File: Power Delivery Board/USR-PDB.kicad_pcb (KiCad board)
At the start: 2 copper layers, 100 x 150 mm, 19 parts, among them U10 Anderson PP45 Vert. 2x1, U11 Anderson PP45 Vert. 2x1, U12 TL2575HV-05IKV, U13 MCP3002-I/P, U2 LM2676T-12_NOPB, U5 Anderson PP45 Vert. 2x1, U6 Anderson PP45 Vert. 2x1, U7 Anderson PP45 Vert. 2x1, U8 Anderson PP45 Vert. 2x1, U9 Anderson PP45 Vert. 2x1

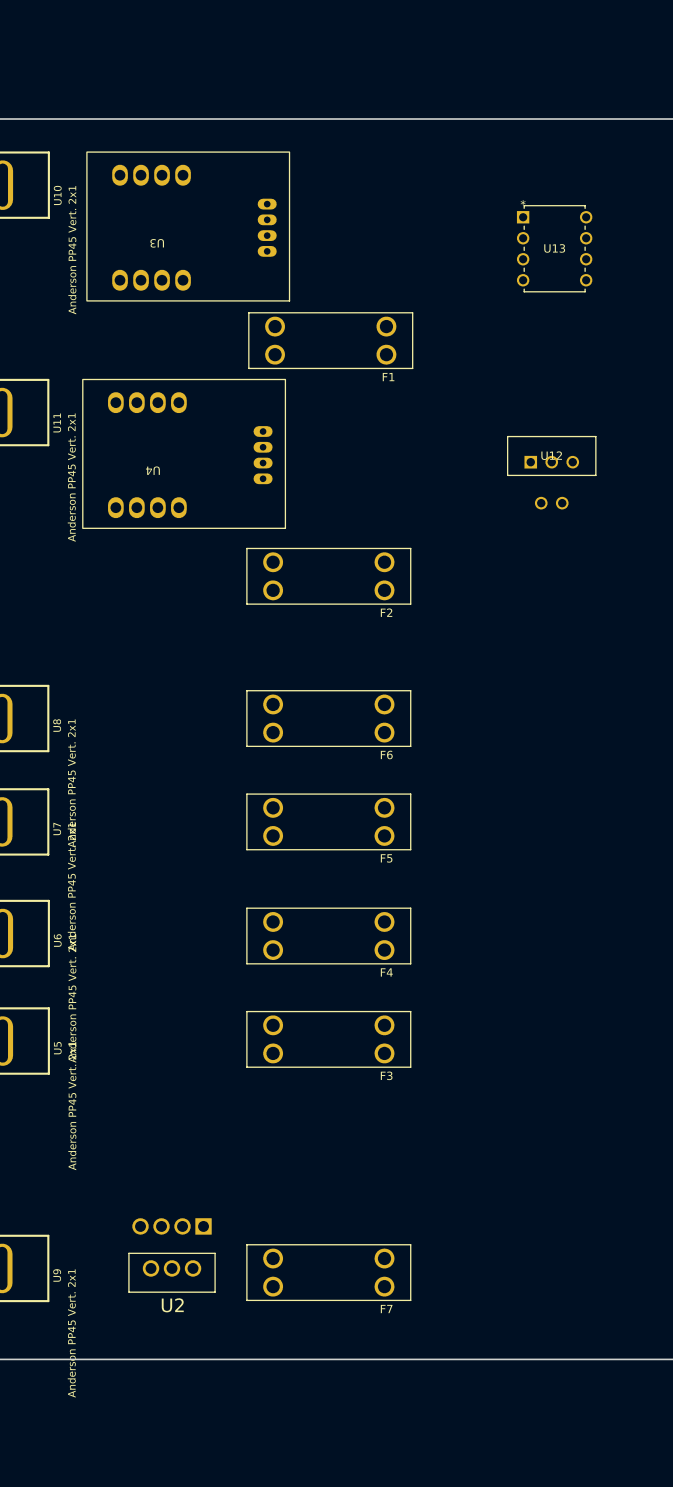
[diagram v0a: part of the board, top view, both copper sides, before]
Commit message: PDB: added footprint for D2
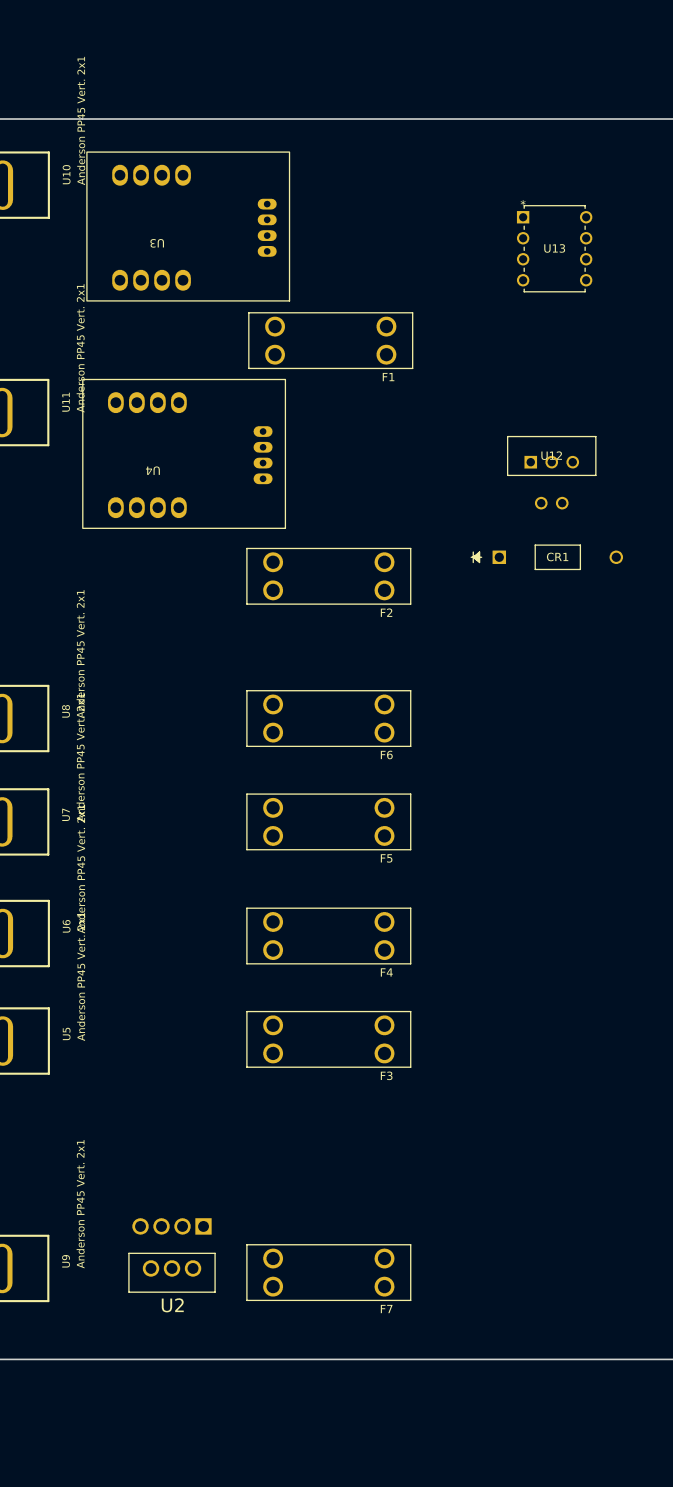
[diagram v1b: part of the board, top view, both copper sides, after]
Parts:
- added CR1: 1N5819, USR:DO-41_STM, F.Cu at (133.9, 75.5)
- F1, F2, F3, F4, F5, F6, F7: footprint USR-Footprint-Library:FUSE_3557-15 -> USR:FUSE_3557-15
- U10, U11, U5, U6, U7, U8, U9: footprint USR-Footprint-Library:ANDERSON PP45 VERT. 2X1 -> USR:ANDERSON PP45 VERT. 2X1
- U12: footprint USR-Footprint-Library:TL2575HV-05IKV -> USR:TL2575HV-05IKV
- U13: footprint USR-Footprint-Library:PDIP8_300MC_MCH -> USR:PDIP8_300MC_MCH
- U2: footprint USR-Footprint-Library:LM2676-TO127P457X1016X2052-7P -> USR:LM2676-TO127P457X1016X2052-7P
- U3, U4: footprint USR-Footprint-Library:LKSR 50-NP -> USR:LKSR 50-NP
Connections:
- net 5Vout renamed 5V

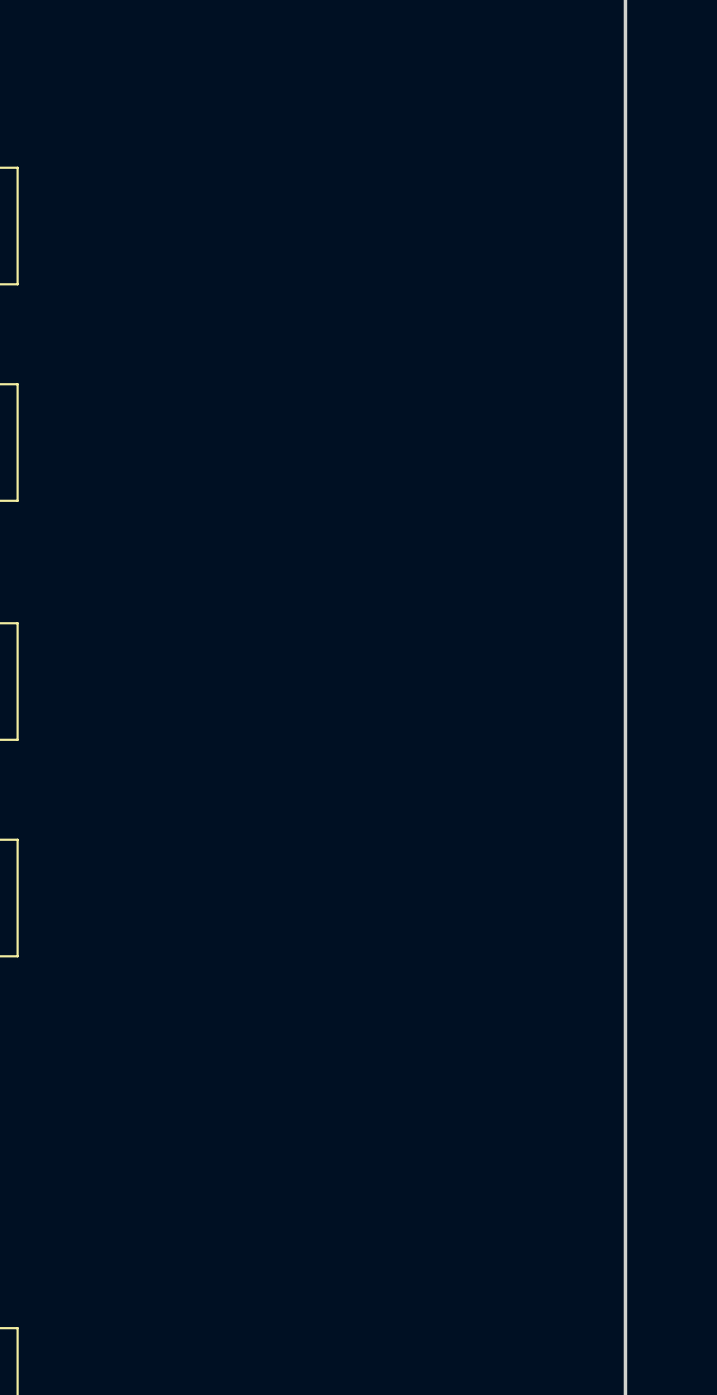
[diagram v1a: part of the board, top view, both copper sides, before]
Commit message: Added footprints and datasheets for capacitors, inductors, and diodes
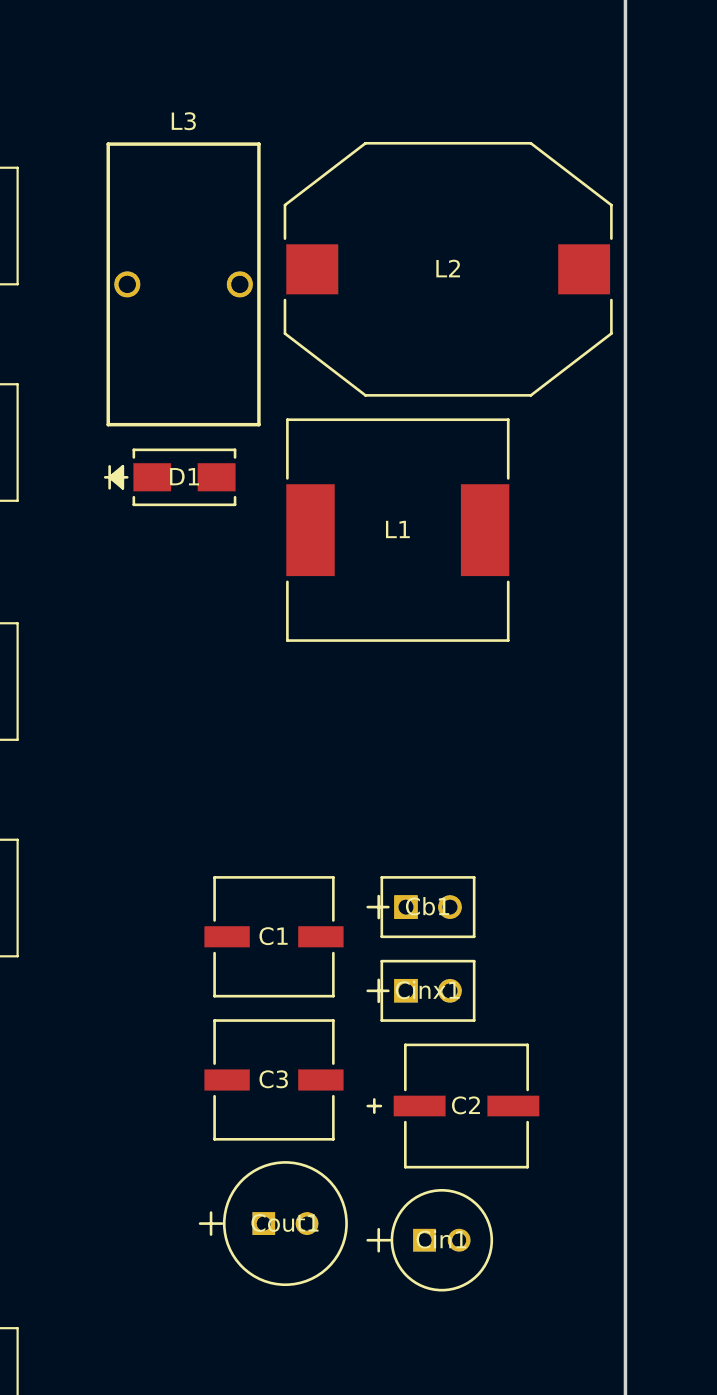
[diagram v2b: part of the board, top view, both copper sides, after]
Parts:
- added C1: 100uF, USR:U2-K_NCH, F.Cu at (137.9, 136.0)
- added C2: 330uF, USR:PCAP_6.3x7.7-ELECT_NCA, F.Cu at (149.1, 145.8)
- added C3: 100uF, USR:U2-K_NCH, F.Cu at (137.9, 144.3)
- added Cb1: 10nF, USR:CAP_C320C_MOLDED RADIAL_KEM, F.Cu at (145.6, 134.3)
- added Cin1: 56uF, USR:CAP_WCAP-ATUL_05.0X11.0_WRE, F.Cu at (146.6, 153.6)
- added Cinx1: 100nF, USR:CAP_C320C_MOLDED RADIAL_KEM, F.Cu at (145.6, 139.2)
- added Cout1: 82uF, USR:CAP_ATLL_06p3X15p0_WRE, F.Cu at (137.4, 152.6)
- added D1: 700mV 2A, USR:SMA_DIO, F.Cu at (132.8, 109.5)
- added L1: 68uH, USR:IND_BOURNS_SRR1210, F.Cu at (145.1, 112.6)
- added L2: 330uH, USR:IND_BOURNS_SDR1806, F.Cu at (148.0, 97.5)
- added L3: 20uH, USR:WE-FI_7447025, F.Cu at (132.7, 98.4)

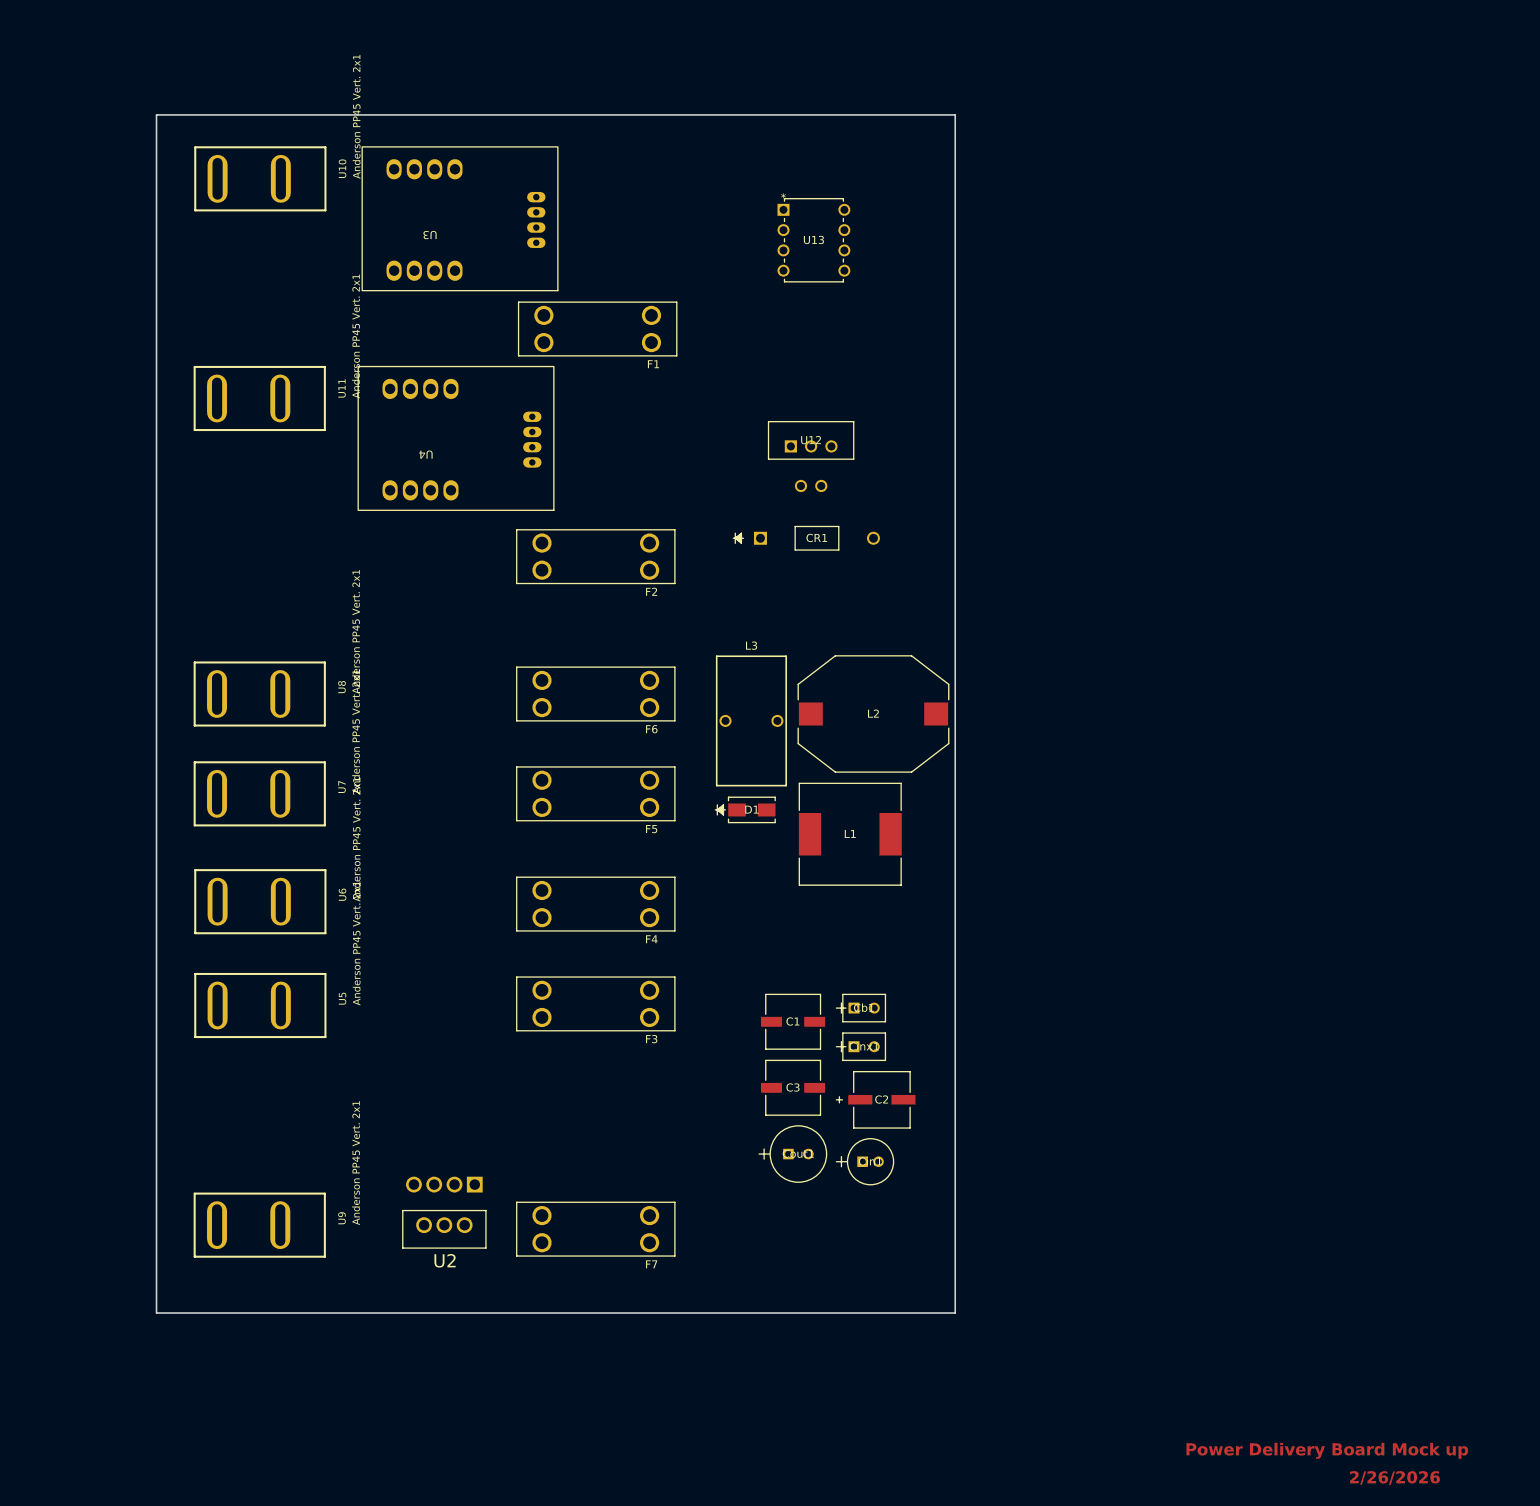
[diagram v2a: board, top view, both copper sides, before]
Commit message: adjusted PCB layout for Power delivery board
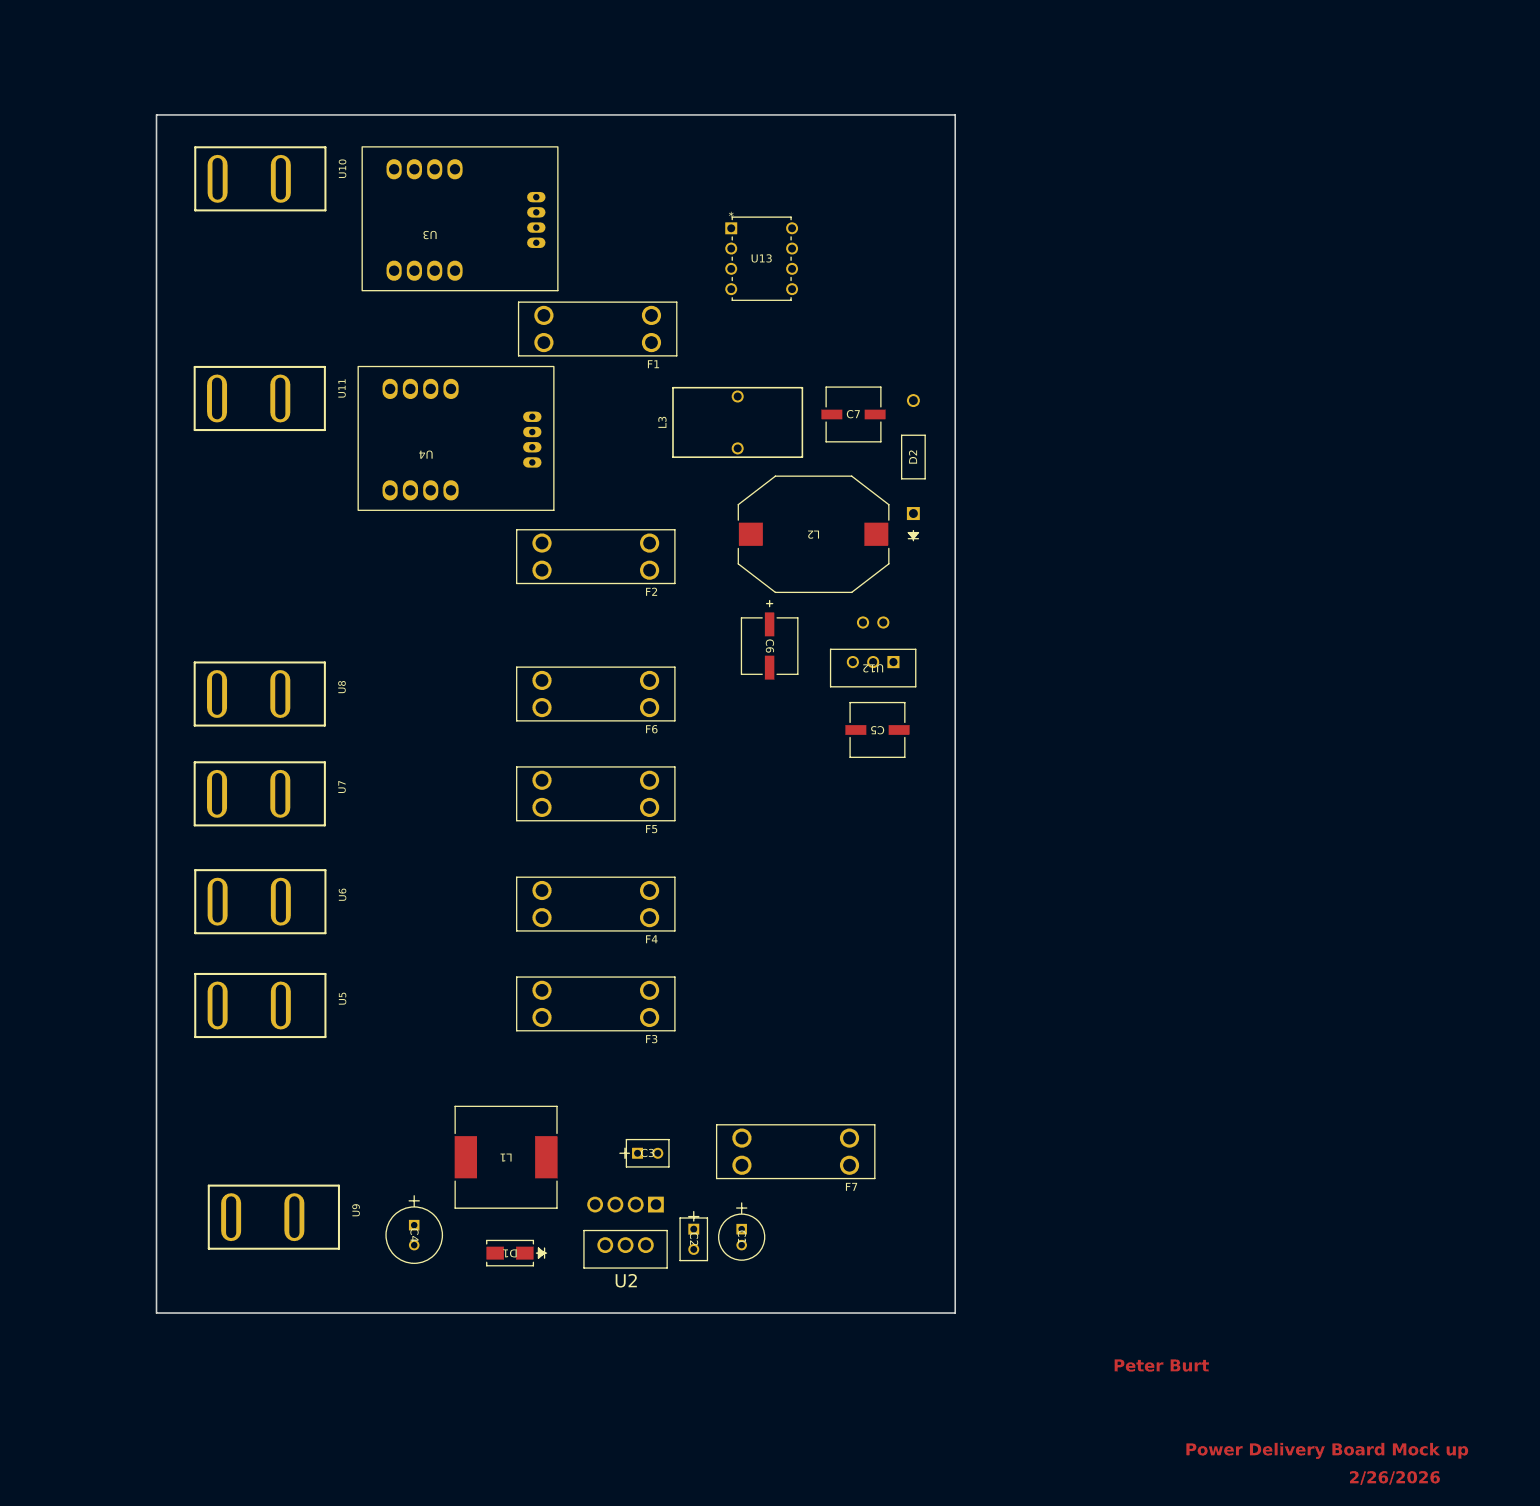
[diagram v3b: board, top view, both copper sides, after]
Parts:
- moved C7 84.6 mm to (145.5, 60.0)
- moved D1 63.2 mm to (102.5, 165.0), turned to 180 degrees
- moved L1 59.1 mm to (102.0, 153.0), turned to 180 degrees
- moved C6 58.5 mm to (135.0, 89.0), turned to -90 degrees
- moved C4 47.7 mm to (90.5, 161.5), turned to -90 degrees
- moved C5 38.0 mm to (148.5, 99.5), turned to 180 degrees
- moved L3 37.4 mm to (131.0, 61.0), turned to 90 degrees
- moved C3 32.6 mm to (118.5, 152.5)
- moved C2 30.4 mm to (125.5, 162.0), turned to -90 degrees
- moved U12 30.1 mm to (145.4, 92.5), turned to 180 degrees
- moved F7 26.8 mm to (138.3, 152.3)
- moved L2 23.7 mm to (140.5, 75.0), turned to 180 degrees
- moved U2 22.8 mm to (113.2, 170.1)
- moved D2 19.4 mm to (153.0, 72.4), turned to 90 degrees
- moved C1 17.3 mm to (131.5, 162.0), turned to -90 degrees
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- renumbered Cin1 to C1, Cinx1 to C2, Cb1 to C3, Cout1 to C4, C1 to C5, C2 to C6, C3 to C7, CR1 to D2
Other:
- board text added: "Peter Burt"
